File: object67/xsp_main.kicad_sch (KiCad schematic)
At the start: 0 parts

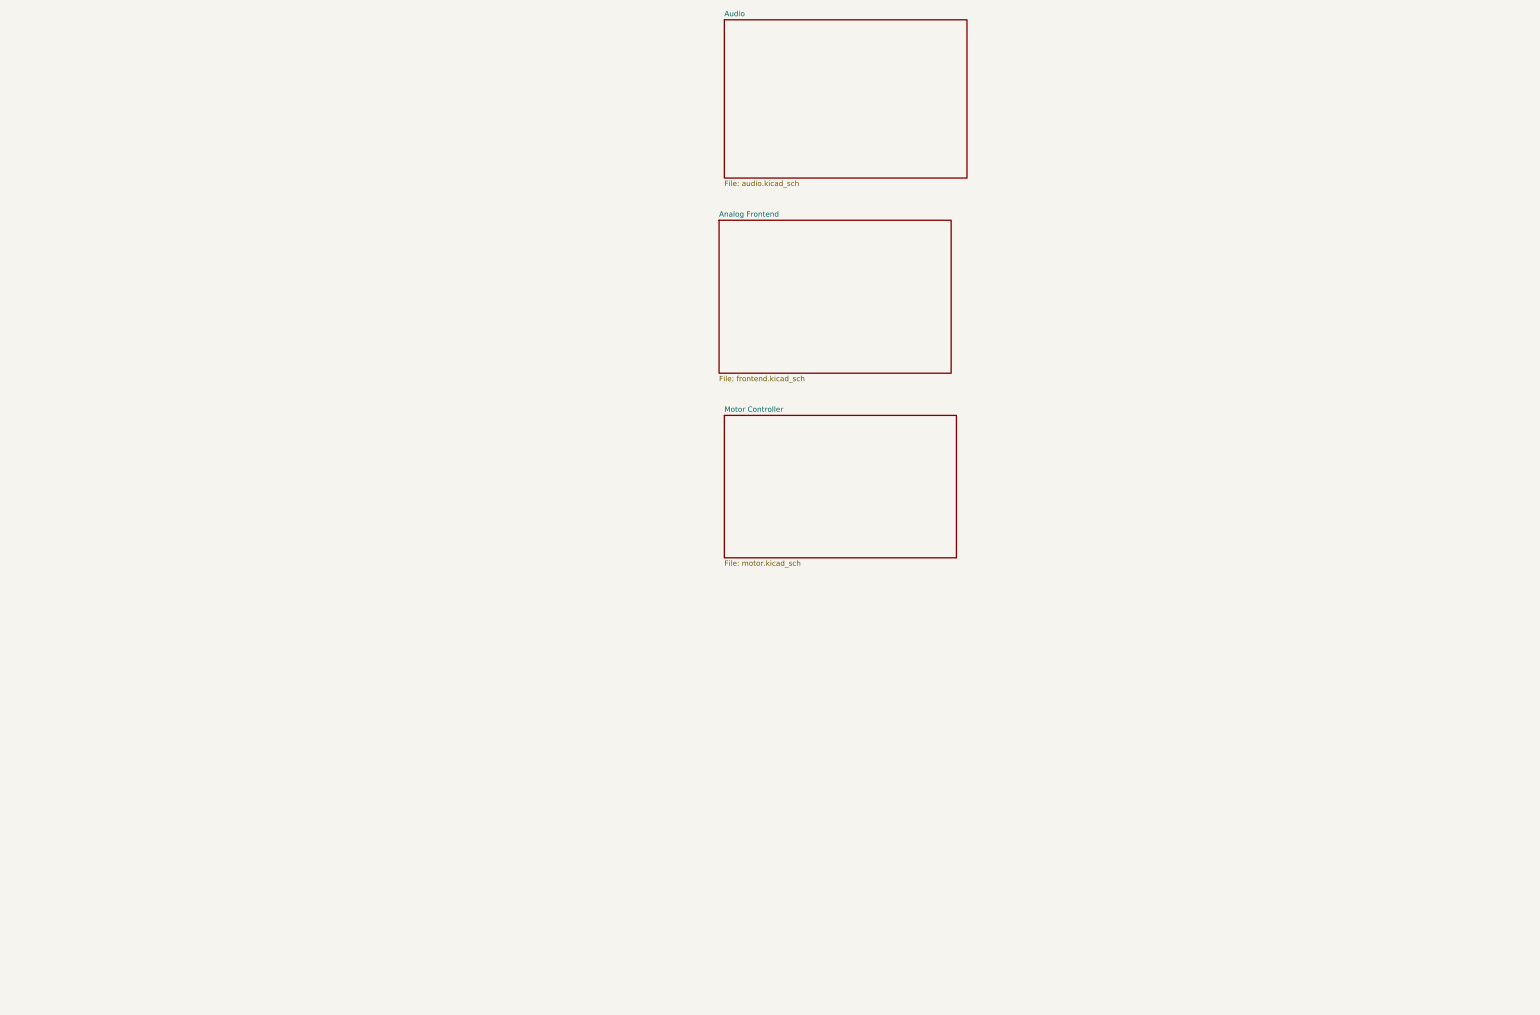
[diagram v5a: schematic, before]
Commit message: Switching power supply
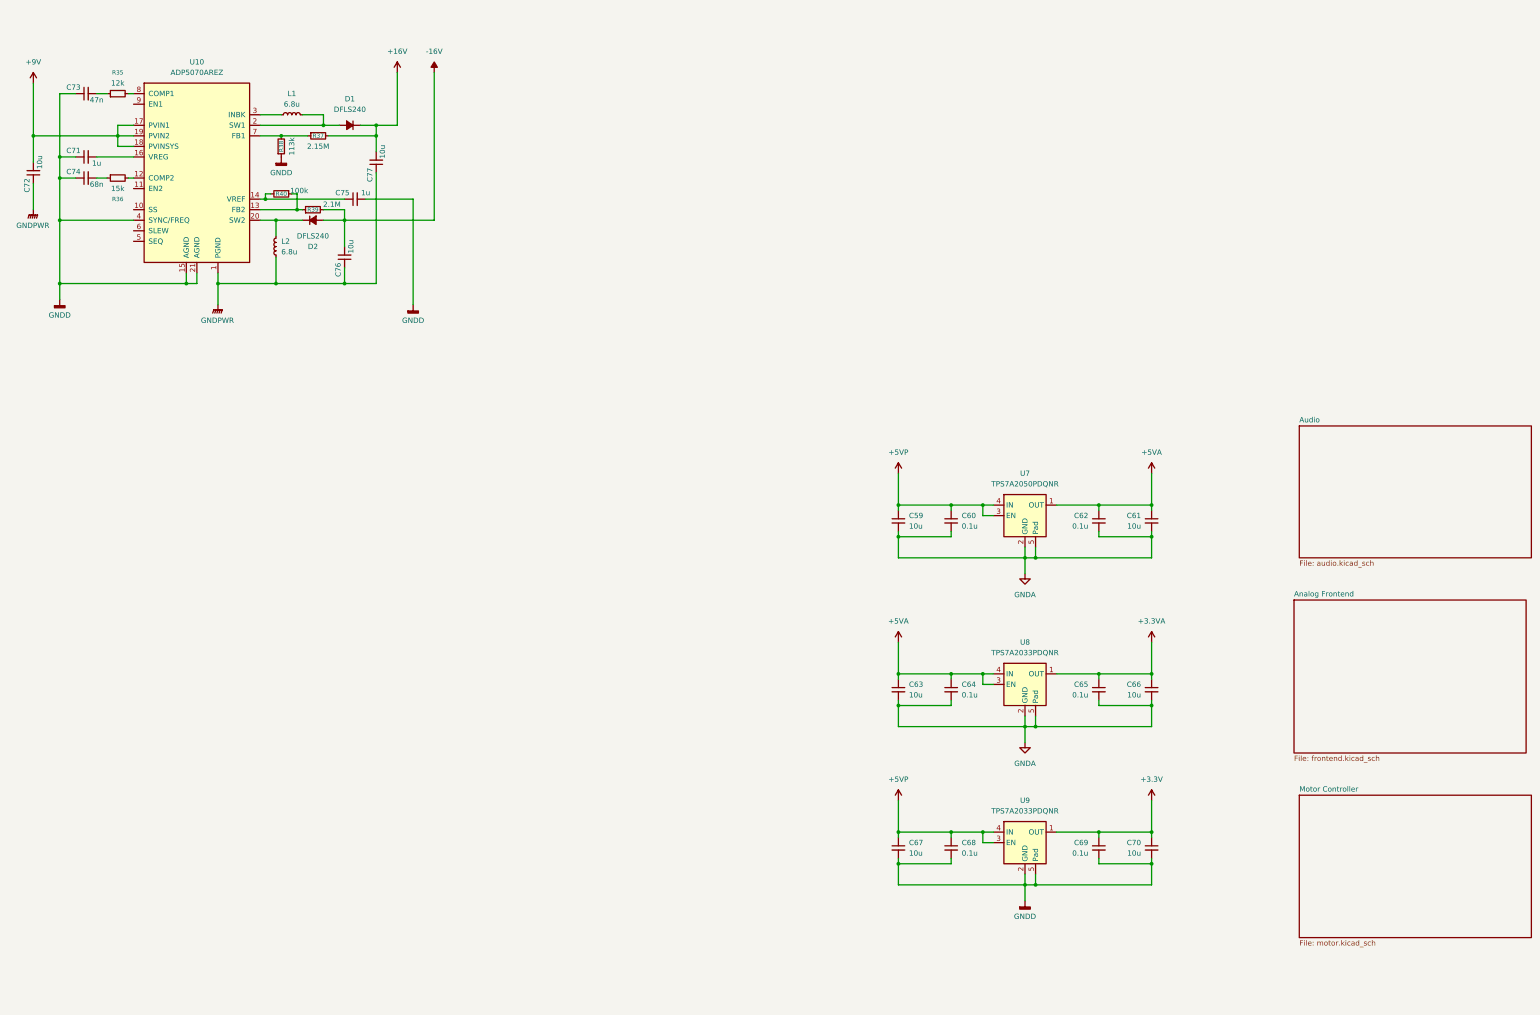
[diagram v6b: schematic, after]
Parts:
- added C59, C61, C63, C66, C67, C70, C72, C76, C77: 10u, symbol Device:C_Small
- added C60, C62, C64, C65, C68, C69: 0.1u, symbol Device:C_Small
- added C71, C75: 1u, symbol Device:C_Small
- added C73: 47n, symbol Device:C_Small
- added C74: 68n, symbol Device:C_Small
- added D1, D2: DFLS240, symbol Device:D_Small_Filled
- added L1, L2: 6.8u, symbol Device:L_Small
- added R35: 12k, symbol Device:R_Small
- added R36: 15k, symbol Device:R_Small
- added R37: 2.15M, symbol Device:R_Small
- added R38: 113k, symbol Device:R_Small
- added R39: 2.1M, symbol Device:R_Small
- added R40: 100k, symbol Device:R_Small
- added U10: ADP5070AREZ, Package_SO:ETSSOP-20-1EP_4.4x6.5mm_P0.65mm_EP3x4.2mm, symbol Regulator_Switching:ADP5070AREZ
- added U7: TPS7A2050PDQNR, Package_SON:Texas_X2SON-4_1x1mm_P0.65mm, symbol Regulator_Linear:TPS7A20xxxDQN
- added U8, U9: TPS7A2033PDQNR, Package_SON:Texas_X2SON-4_1x1mm_P0.65mm, symbol Regulator_Linear:TPS7A20xxxDQN
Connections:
- new net: D1.2 (A), L1.2, U10.2 (SW1)
- new net: C71.2, U10.16 (VREG)
- new net: R39.1, R40.1, U10.13 (FB2)
- new net: C75.1, R40.2, U10.14 (VREF)
- new net: C74.2, R36.1
- new net: R36.2, U10.12 (COMP2)
- new net: D2.1 (K), L2.2, U10.20 (SW2)
- new net: C73.2, R35.1
- new net: R35.2, U10.8 (COMP1)
- new net: R37.1, R38.2, U10.7 (FB1)
- new net: L1.1, U10.3 (INBK)
- new net +16V: C77.2, D1.1 (K), R37.2
- new net +3.3V: C69.1, C70.1, U9.1 (OUT)
- new net +3.3VA: C65.1, C66.1, U8.1 (OUT)
- new net +5VA: C61.1, C62.1, C63.1, C64.1, U7.1 (OUT), U8.3 (EN), U8.4 (IN)
- new net +5VP: C59.1, C60.1, C67.1, C68.1, U7.3 (EN), U7.4 (IN), U9.3 (EN), U9.4 (IN)
- new net +9V: C72.2, U10.17 (PVIN1), U10.18 (PVINSYS), U10.19 (PVIN2)
- new net -16V: C76.2, D2.2 (A), R39.2
- new net GNDA: C59.2, C60.2, C61.2, C62.2, C63.2, C64.2, C65.2, C66.2, U7.2 (GND), U7.5 (Pad), U8.2 (GND), U8.5 (Pad)
- new net GNDD: C67.2, C68.2, C69.2, C70.2, C71.1, C73.1, C74.1, C75.2, R38.1, U10.15 (AGND), U10.21 (AGND), U10.4 (SYNC/FREQ), U9.2 (GND), U9.5 (Pad)
- new net GNDPWR: C72.1, C76.1, C77.1, L2.1, U10.1 (PGND)
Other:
- title: (none) -> Power and Distribution Board

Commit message: LDO
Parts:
- added C78, C79: 10u, symbol Device:C_Small
- added C80: 2.2n, symbol Device:C_Small
- added C81: 470n, symbol Device:C_Small
- added C82, C83, C84, C85, C86: 22u, symbol Device:C_Small
- added C87, C89: 1u, symbol Device:C_Small
- added C88, C91, C93: 2.2u, symbol Device:C_Small
- added C90: 1n, symbol Device:C_Small
- added C92: 0.1u, symbol Device:C_Small
- added FB4: 8R, symbol Device:FerriteBead_Small
- added L3: 2.2u, symbol Device:L_Small
- added R41: 7.5k, symbol Device:R_Small
- added R42: 27k, symbol Device:R_Small
- added R43: 4.7k, symbol Device:R_Small
- added R44: 20k, symbol Device:R_Small
- added R45: 10k, symbol Device:R_Small
- added R46: 1k, symbol Device:R_Small
- added R47: 52.3k, symbol Device:R_Small
- added R48, R49: 4.64k, symbol Device:R_Small
- added U11: TPS62912, Package_DFN_QFN:Texas_RPU0010A_VQFN-HR-10_2x2mm_P0.5mm, symbol Regulator_Switching:TPS62912
- added U12: ADP7142ARDZ, Package_SO:SOIC-8-1EP_3.9x4.9mm_P1.27mm_EP2.29x3mm, symbol Regulator_Linear:ADP7142ARDZ
- added U13: ADP7182AUJZ, Package_TO_SOT_SMD:TSOT-23-5, symbol Regulator_Linear:ADP7182AUJZ
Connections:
- net +5VP: no longer C59.1, C60.1, U7.3 (EN), U7.4 (IN)
- net +9V: now also C78.2, C79.2, C80.2, U11.1 (EN/SYNC), U11.6 (VIN)
- net GNDA: now also C87.1, C88.1, C90.1, C91.1, C93.1, R45.1, R48.1, U12.4 (GND), U12.9 (GND), U13.1 (GND)
- net GNDPWR: now also C78.1, C79.1, C80.1, C81.1, C82.1, C83.1, C84.1, C85.1, C86.1, R41.1, R43.1, U11.4 (PGND), U11.7 (PSNS)
- new net: C81.2, U11.8 (NR/SS)
- new net: C82.2, C83.2, C84.2, FB4.1, L3.2, U11.3 (VO)
- new net: C89.2, C91.2, R44.2, U12.1 (VOUT), U12.2 (VOUT)
- new net: R44.1, R45.2, R46.2, U12.3 (SENSE/ADJ)
- new net: C90.2, U12.6 (SS)
- new net: C87.2, U12.7 (VIN), U12.8 (VIN)
- new net: C89.1, R46.1
- new net: L3.1, U11.2 (SW)
- new net: R47.1, R48.2, R49.2, U13.4 (ADJ)
- new net: R41.2, U11.10 (S-CONF)
- new net: C92.2, C93.2, R47.2, U13.5 (VOUT)
- new net: R42.1, R43.2, U11.9 (FB)
- new net: C92.1, R49.1
- new net: C88.2, U13.2 (VIN)
- new net +5.39574468085V: C59.1, C60.1, C85.2, C86.2, FB4.2, R42.2, U7.3 (EN), U7.4 (IN)

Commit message: Add LDO
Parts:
- removed R46: 1k, symbol Device:R_Small
- removed R47: 52.3k, symbol Device:R_Small
- removed R48, R49: 4.64k, symbol Device:R_Small
- removed U12: ADP7142ARDZ, Package_SO:SOIC-8-1EP_3.9x4.9mm_P1.27mm_EP2.29x3mm, symbol Regulator_Linear:ADP7142ARDZ
- removed U13: ADP7182AUJZ, Package_TO_SOT_SMD:TSOT-23-5, symbol Regulator_Linear:ADP7182AUJZ
- added IC5: TPS7A4701RGWT, object67:QFN65P500X500X100-21N-D, symbol object67:TPS7A4701RGWT
- added IC6: TPS7A3301RGWR, object67:QFN65P500X500X100-21N-D, symbol object67:TPS7A3301RGWR
- added J2: PJ-037A, object67:PJ037A, symbol object67:PJ-037A
- added J3: Power In, symbol Connector:Conn_01x02_Pin
- added J4: 216700-0249, 2167000249, symbol object67:216700-0249
- added TP1, TP2, TP3, TP4: TestPoint, symbol Connector:TestPoint
- C61, C66, C70: value 10u -> 47u
- C88: value 2.2u -> 10u
- C89: value 1u -> 10u
- C90: value 1n -> 47u
- C91: value 2.2u -> 10n
- C92: value 0.1u -> 1u
- C93: value 2.2u -> 47u
- R44: value 20k -> 1.24M
- R45: value 10k -> 105k
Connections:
- net +16V: now also C88.1, IC5.13 (EN), IC5.15 (IN_1), IC5.16 (IN_2), TP1.1, TP3.1
- net +9V: now also J2.2, J3.1 (Pin_1)
- net -16V: now also C89.1, IC6.13 (EN), IC6.15 (IN_1), IC6.16 (IN_2), TP2.1, TP4.1
- net GNDA: now also C88.2, C89.2, C90.2, C92.1, C93.2, IC5.21 (GND_2), IC5.4 (6P4V2), IC5.5 (6P4V1), IC5.7 (GND_1), IC5.9 (0P8V); no longer C88.1, C90.1, C91.1, C93.1
- net GNDPWR: now also J2.1, J3.2 (Pin_2)
- net at R44.1, R45.2: now also C91.2, IC6.3 (FB)
- net at C87.2: now also IC5.14 (NR)
- net at C92.2: now also IC6.14 (NR/SS); no longer C93.2
- new net +15V: C90.1, IC5.1 (OUT_1), IC5.20 (OUT_2), IC5.3 (SENSE/FB)
- new net -15V: C91.1, C93.1, IC6.1 (OUT_1), IC6.20 (OUT_2), R44.2
- no-connect marks 0 -> 22
